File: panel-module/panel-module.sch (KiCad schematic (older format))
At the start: 11 parts, among them J1 East, J2 West, J3 Debug, SW1 Setup, SW2 Reset

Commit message: Introduce new serial numbering scheme
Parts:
- R1: Price (none) -> 0.16; Product (none) -> https://www.mouser.de/ProductDetail/YAGEO/RT1206FRE07220RL?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
- R2: Price (none) -> 0.16; Product (none) -> https://www.mouser.de/ProductDetail/YAGEO/RT1206FRE0710KL?q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
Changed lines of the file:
@@
 encoding utf-8
 Sheet 1 1
-Title ""
-Date ""
-Rev ""
-Comp ""
-Comment1 ""
+Title "Satellite Panel"
+Date "2022-02-08"
+Rev "2.0"
+Comp "GrayC GmbH"
+Comment1 "Fabian Schlegel"
 Comment2 ""
 Comment3 ""
-Comment4 ""
+Comment4 "Front Panel Module with Setup / Reset Buttons and Status LEDs"
 $EndDescr
 $Comp
@@
 F 1 "220R" H 2670 3755 50  0000 L CNN
 F 2 "Resistor_SMD:R_1206_3216Metric_Pad1.30x1.75mm_HandSolder" V 2530 3800 50  0001 C CNN
-F 3 "~" H 2600 3800 50  0001 C CNN
+F 3 "https://www.mouser.de/datasheet/2/447/PYu_RT_1_to_0_01_RoHS_L_11-1669912.pdf" H 2600 3800 50  0001 C CNN
+F 4 "https://www.mouser.de/ProductDetail/YAGEO/RT1206FRE07220RL?qs=yNCrj0CQcyIDJm%252BN6MoQJw%3D%3D" H 2600 3800 50  0001 C CNN "Product"
+F 5 "0.16" H 2600 3800 50  0001 C CNN "Price"
 	1    2600 3800
 	1    0    0    -1
@@
 F 1 "10k" H 3320 3755 50  0000 L CNN
 F 2 "Resistor_SMD:R_1206_3216Metric_Pad1.30x1.75mm_HandSolder" V 3180 3800 50  0001 C CNN
-F 3 "~" H 3250 3800 50  0001 C CNN
+F 3 "https://www.mouser.de/datasheet/2/447/PYu_RT_1_to_0_01_RoHS_L_11-1669912.pdf" H 3250 3800 50  0001 C CNN
+F 4 "https://www.mouser.de/ProductDetail/YAGEO/RT1206FRE0710KL?qs=8cPjvKtxWv45%2FSPYTvTNKg%3D%3D" H 3250 3800 50  0001 C CNN "Product"
+F 5 "0.16" H 3250 3800 50  0001 C CNN "Price"
 	1    3250 3800
 	1    0    0    -1

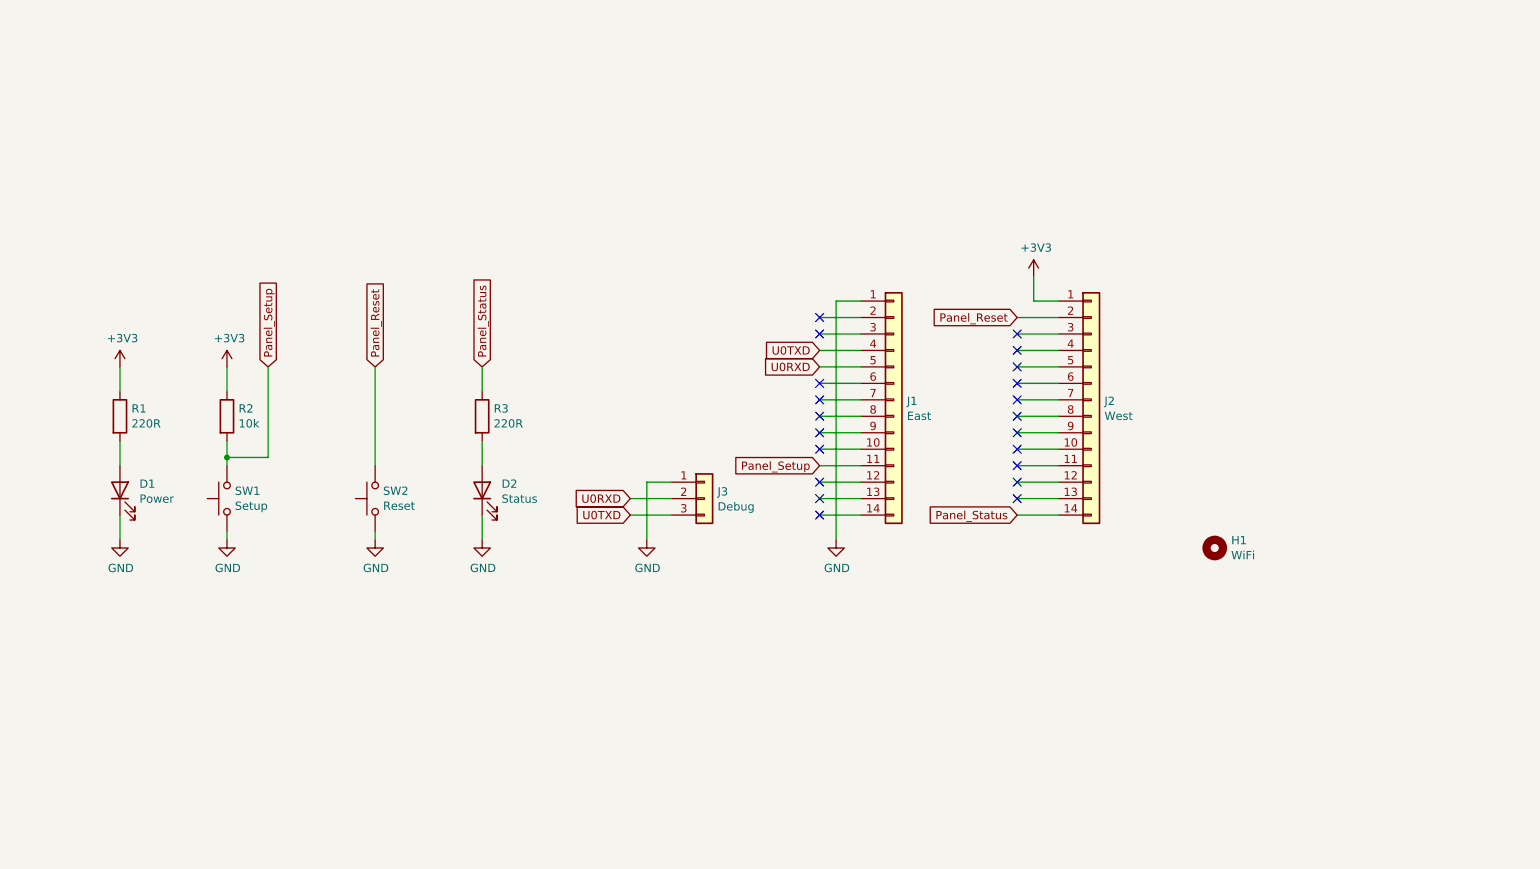
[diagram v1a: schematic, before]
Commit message: Work on Ethernet module
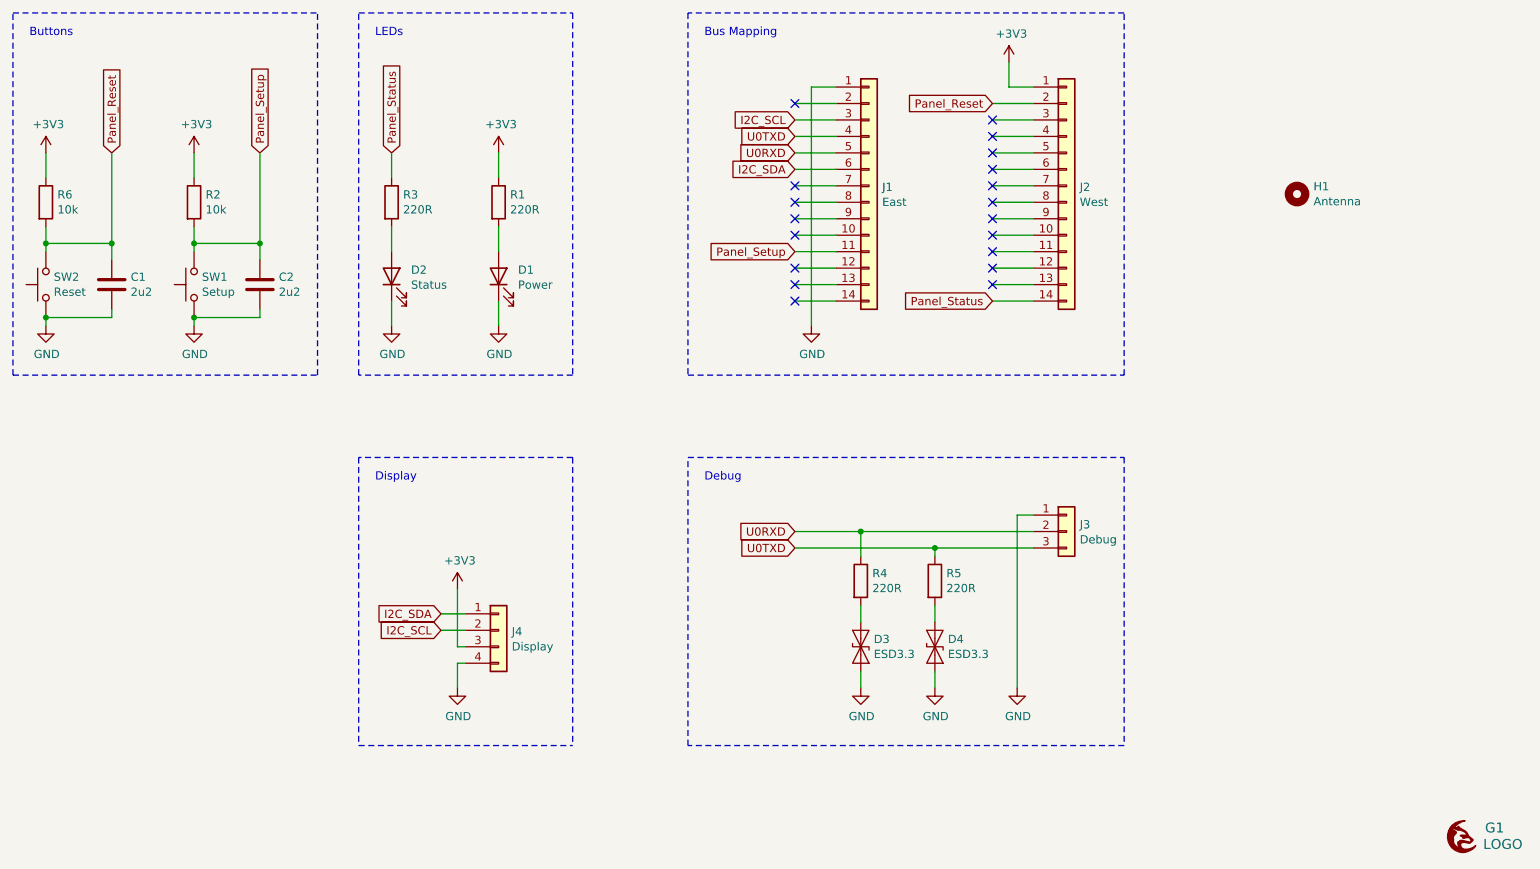
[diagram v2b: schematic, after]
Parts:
- added C1, C2: 2u2, Capacitor_SMD:C_1206_3216Metric_Pad1.33x1.80mm_HandSolder, symbol Device:C
- added D3, D4: ESD3.3, Resistor_SMD:R_0603_1608Metric_Pad0.98x0.95mm_HandSolder, symbol Diode:ESD9B3.3ST5G
- added G1: LOGO, images:grayc-logo-negative, symbol grayc-logo-negative:LOGO
- added J4: Display, Connector_PinHeader_2.54mm:PinHeader_1x04_P2.54mm_Vertical, symbol Connector_Generic:Conn_01x04
- added R4, R5: 220R, Resistor_SMD:R_1206_3216Metric_Pad1.30x1.75mm_HandSolder, symbol Device:R
- added R6: 10k, Resistor_SMD:R_1206_3216Metric_Pad1.30x1.75mm_HandSolder, symbol Device:R
- D1, D2: footprint LED_SMD:LED_1206_3216Metric_Pad1.42x1.75mm_HandSolder -> footprints:LED_1206_3216Metric_Pad1.42x1.75mm_HandSolder_With_Cover; Price (none) -> 0.06; Product (none) -> https://www.mouser.de/ProductDetail/Lite-On/LTST-C150GKT
- H1: value WiFi -> Antenna; footprint MountingHole:MountingHole_5.5mm -> footprints:MountingHole_5.5mm_No_Bound; Price (none) -> 0; Product (none) -> N/A
- J1, J2, J3: Price (none) -> 0; Product (none) -> N/A
- R1: Price 0.16 -> 0.08; Product https://www.mouser.de/ProductDetail/YAGEO/RT1206FRE07220RL?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 -> https://www.mouser.de/ProductDetail/Vishay-Draloric/RCG1206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
- R3: Price (none) -> 0.08; Product (none) -> https://www.mouser.de/ProductDetail/Vishay-Draloric/RCG1206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
- SW1, SW2: Price (none) -> 0.47; Product (none) -> https://www.mouser.de/ProductDetail/CK/PTS645SK43SMTR92LFS
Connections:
- net +3V3: now also J4.3 (Pin_3), R6.1
- net GND: now also C1.2, C2.2, D3.2 (A2), D4.2 (A2), J4.4 (Pin_4)
- net Panel_Reset: now also C1.1, R6.2
- net Panel_Setup: now also C2.1
- net U0RXD: now also R4.1
- net U0TXD: now also R5.1
- net I2C_SCL: now reaches J1.3 (Pin_3)
- net I2C_SCL: now also J4.2 (Pin_2)
- net I2C_SDA: now reaches J1.6 (Pin_6)
- net I2C_SDA: now also J4.1 (Pin_1)
- new net: D4.1 (A1), R5.2
- new net: D3.1 (A1), R4.2
- no-connect marks 21 -> 19
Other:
- note added: "Bus Mapping"
- note added: "Buttons"
- note added: "Debug"
- note added: "Display"
- note added: "LEDs"
- moved on the sheet: D1, D2, H1, J1, J2, J3, R1, R2, R3, SW1, SW2

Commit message: Added Panel Module to build
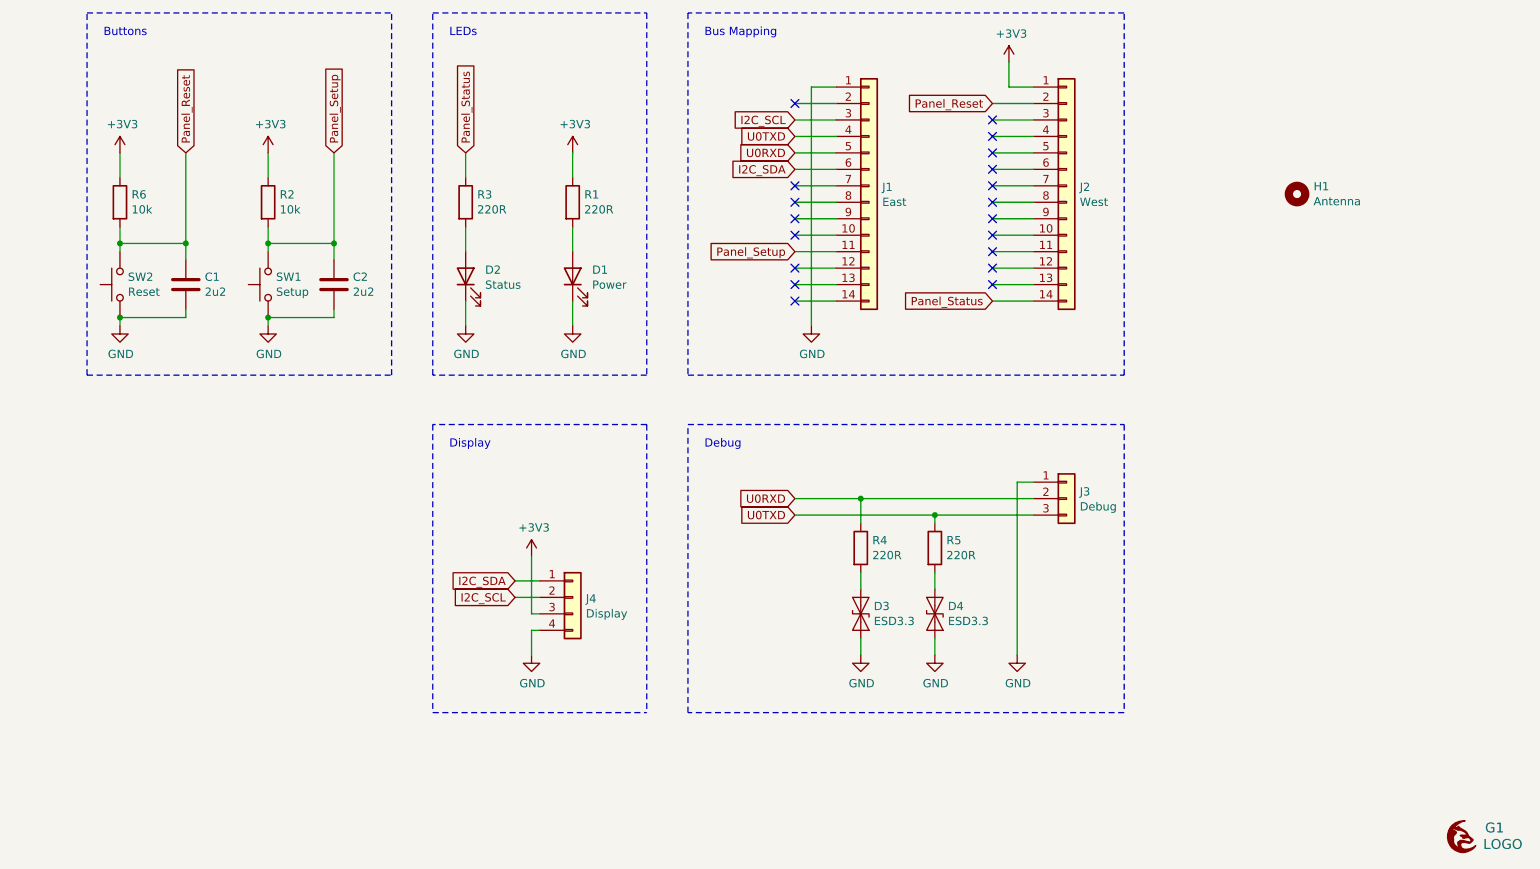
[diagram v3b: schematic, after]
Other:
- moved on the sheet: C1, C2, D1, D2, D3, D4, J3, J4, R1, R2, R3, R4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

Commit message: Added OpenHardware Logo to PCBs
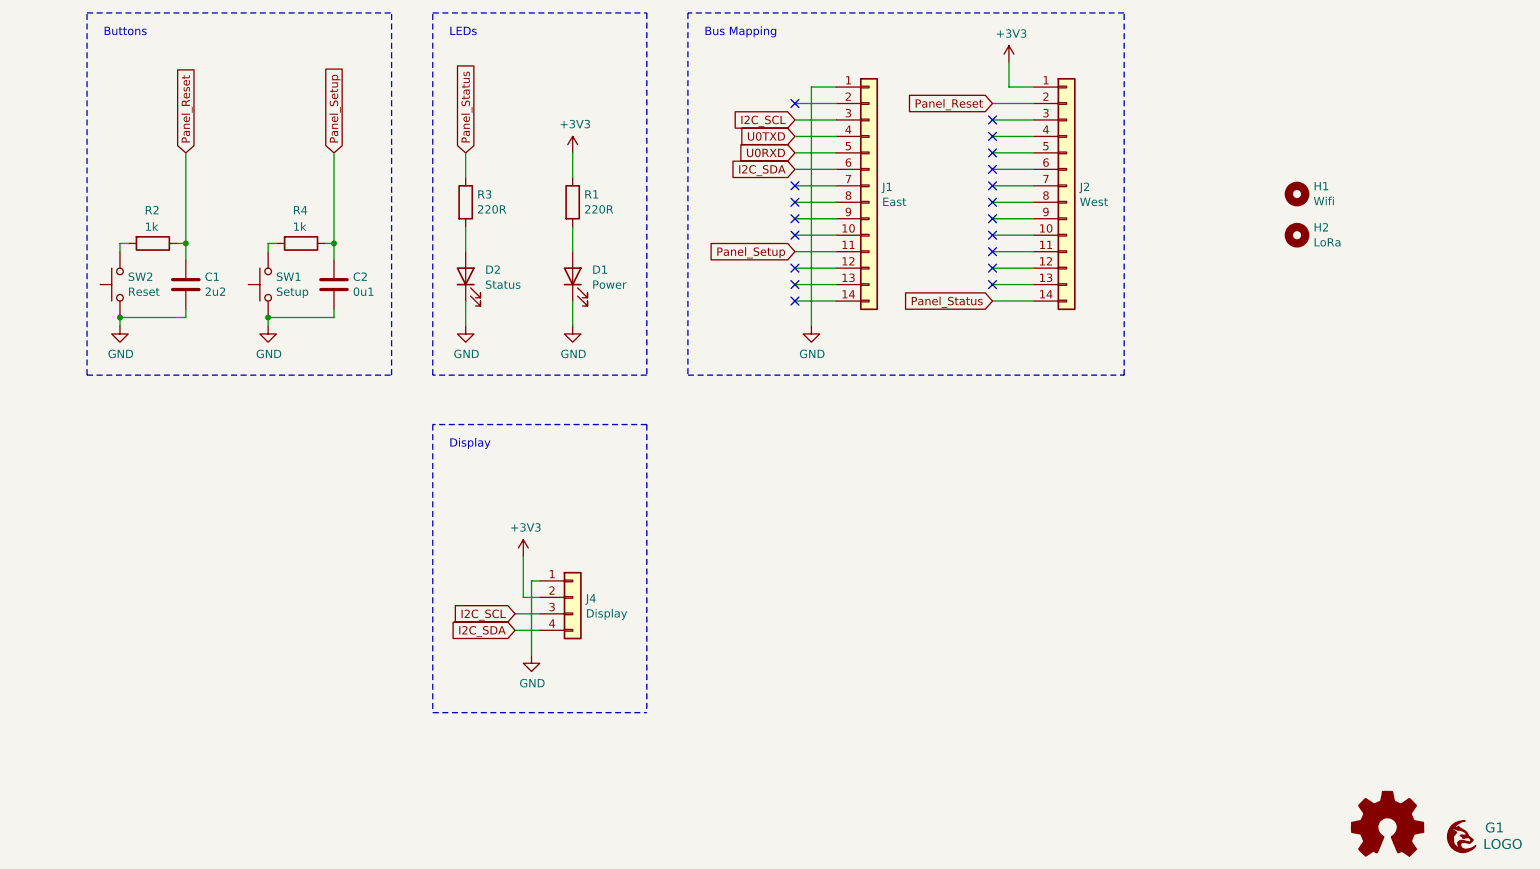
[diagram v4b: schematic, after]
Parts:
- removed D3, D4: ESD3.3, Resistor_SMD:R_0603_1608Metric_Pad0.98x0.95mm_HandSolder, symbol Diode:ESD9B3.3ST5G
- removed J3: Debug, Connector_PinHeader_2.54mm:PinHeader_1x03_P2.54mm_Horizontal, symbol Connector_Generic:Conn_01x03
- removed R5: 220R, Resistor_SMD:R_1206_3216Metric_Pad1.30x1.75mm_HandSolder, symbol Device:R
- removed R6: 10k, Resistor_SMD:R_1206_3216Metric_Pad1.30x1.75mm_HandSolder, symbol Device:R
- added G2: Logo_Open_Hardware_Small, Symbol:OSHW-Logo2_7.3x6mm_SilkScreen, symbol Graphic:Logo_Open_Hardware_Small
- added H2: LoRa, MountingHole:MountingHole_6.4mm_M6, symbol Mechanical:MountingHole
- C2: value 2u2 -> 0u1; Price 0.07 -> (none); Product https://www.mouser.de/ProductDetail/Taiyo-Yuden/TMK316BJ225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 -> (none)
- H1: value Antenna -> Wifi; footprint footprints:MountingHole_5.5mm_No_Bound -> MountingHole:MountingHole_6.4mm_M6
- R2: value 10k -> 1k; Price 0.16 -> 0.08; Product https://www.mouser.de/ProductDetail/YAGEO/RT1206FRE0710KL?q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 -> https://www.mouser.de/ProductDetail/Vishay-Draloric/RCG1206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
- R4: value 220R -> 1k
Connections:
- net +3V3: now also J4.2 (Pin_2); no longer J4.3 (Pin_3), R2.1
- net GND: now also J4.1 (Pin_1); no longer J4.4 (Pin_4)
- net I2C_SCL: now also J4.3 (Pin_3); no longer J4.2 (Pin_2)
- net I2C_SDA: now also J4.4 (Pin_4); no longer J4.1 (Pin_1)
- net Panel_Reset: now also R2.1; no longer SW2.2
- net Panel_Setup: now also R4.1; no longer R2.2, SW1.2
- net U0RXD: no longer R4.1
- net at R4.2: now also SW1.2
- new net: R2.2, SW2.2
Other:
- note removed: "Debug"
